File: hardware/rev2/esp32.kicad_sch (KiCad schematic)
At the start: 38 parts, among them J1 SMA, J6 SMA, SW1 SW_Push, SW2 SW_Push, U1 ESP32-S3FN8, Y1 40MHz (±10 ppm, >500 mV)

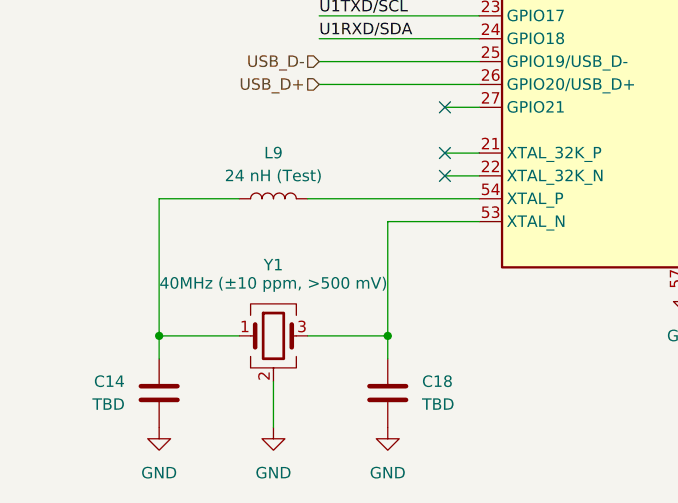
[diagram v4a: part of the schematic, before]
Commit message: added all footprints for esp32 and sx1262, began layouting
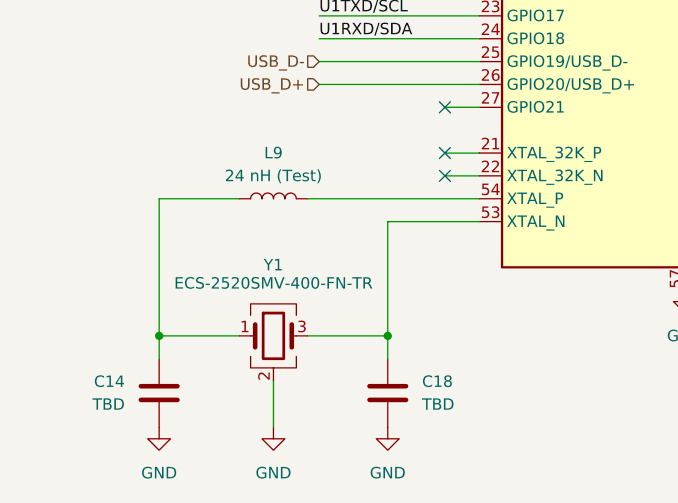
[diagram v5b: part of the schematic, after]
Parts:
- TP1, TP2: footprint (none) -> TestPoint:TestPoint_Pad_D1.0mm
- Y1: value 40MHz (±10 ppm, >500 mV) -> ECS-2520SMV-400-FN-TR; footprint (none) -> Oscillator:Oscillator_SMD_ECS_2520MV-xxx-xx-4Pin_2.5x2.0mm; Mouser Part Number (none) -> 520-EC2520SMV400FNTR

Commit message: continued routing and layouting
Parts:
- renumbered C13 to C11, C17 to C12, C14 to C13, C15 to C14, C21 to C15, C18 to C17, C19 to C18, C20 to C19, C22 to C20, C23 to C21, C24 to C22, C26 to C23, C25 to C24, C27 to C25, J1 to J7, R14 to R10, R15 to R11, R16 to R12, R12 to R13, R19 to R14, R20 to R15, R21 to R16, R4 to R6, R17 to R7, R1 to R8, R13 to R9, SW2 to SW1, SW1 to SW2, U1 to U2

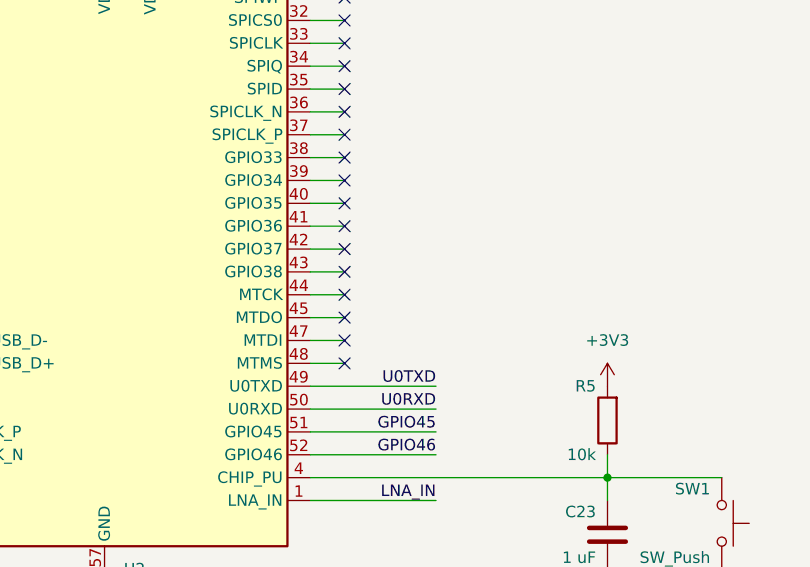
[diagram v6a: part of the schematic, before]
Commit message: finished routing most of the RF and power for SX1262 and ESP32, also decided final ish positions for both.
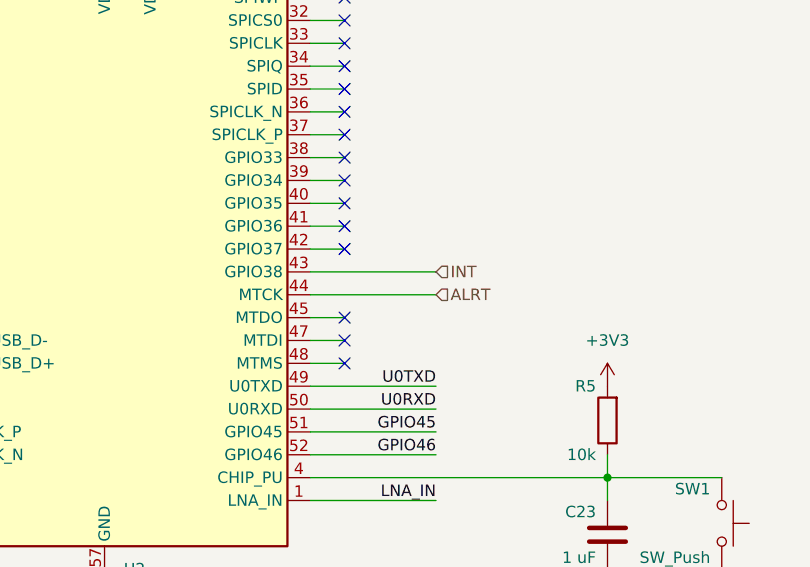
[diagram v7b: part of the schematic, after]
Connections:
- net INT: now reaches U2.43 (GPIO38)
- net ALRT: now reaches U2.44 (MTCK)
- no-connect marks 26 -> 24
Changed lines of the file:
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@@
 	)
 	(no_connect
-		(at 116.84 139.7)
-	)
-	(no_connect
 		(at 116.84 101.6)
 	)
@@
 	)
 	(no_connect
-		(at 116.84 137.16)
-	)
-	(no_connect
 		(at 116.84 147.32)
 	)
@@
 	(wire
 		(pts
-			(xy 113.03 139.7) (xy 116.84 139.7)
+			(xy 113.03 139.7) (xy 127 139.7)
 		)
 		(stroke
@@
 	(wire
 		(pts
-			(xy 113.03 137.16) (xy 116.84 137.16)
+			(xy 113.03 137.16) (xy 127 137.16)
 		)
 		(stroke
@@
 		)
 	)
+	(hierarchical_label "ALRT"
+		(shape input)
+		(at 127 139.7 0)
+		(effects
+			(font
+				(size 1.27 1.27)
+			)
+			(justify left)
+		)
+	)
 	(hierarchical_label "RXD{slash}SDA"
 		(shape input)
@@
 		(effects
 			(font
+				(size 1.27 1.27)
+			)
+			(justify left)
+		)
+	)
+	(hierarchical_label "INT"
+		(shape input)
+		(at 127 137.16 0)
+		(effects
+			(font

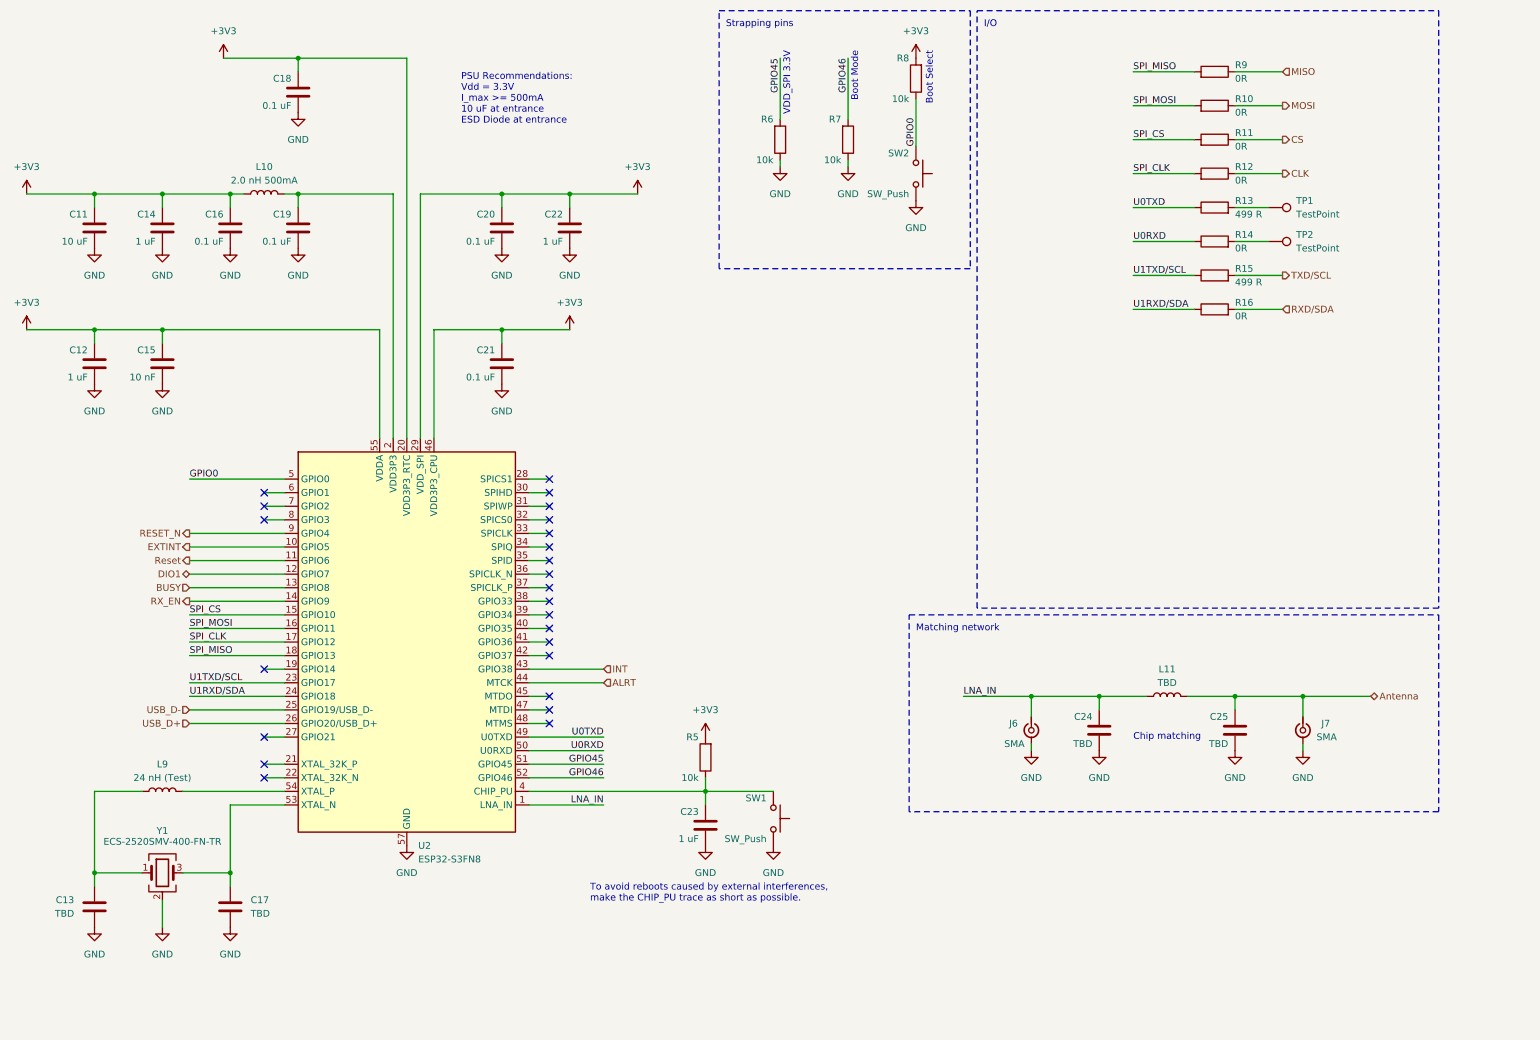
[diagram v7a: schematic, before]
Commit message: routed everything ESP32 and SX1262, will hopefully work. still needs more testpoints
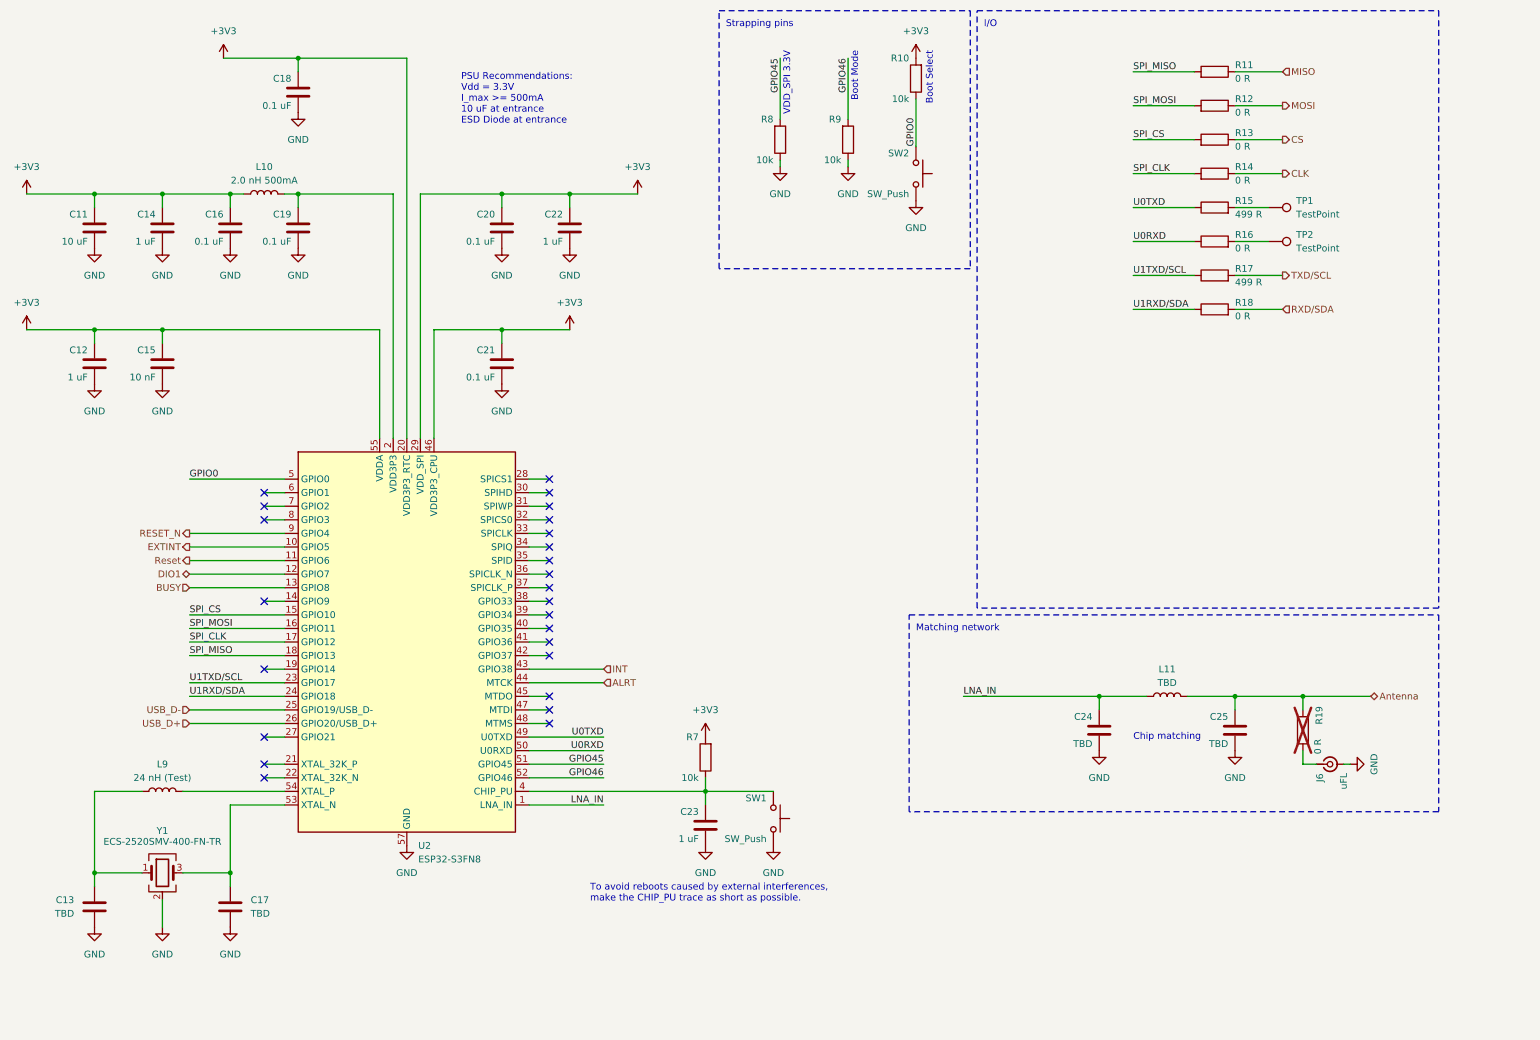
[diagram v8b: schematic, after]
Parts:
- removed J7: SMA, Connector_Coaxial:SMA_Amphenol_132134-16_Vertical, symbol Connector:Conn_Coaxial_Small
- added R19: 0 R, Resistor_SMD:R_0402_1005Metric_Pad0.72x0.64mm_HandSolder, symbol Device:R
- C16, C18, C19, C20, C21: Mouser Part Number 81-GCJ188R71E104KA2D -> 81-GCJ188R71E104KA2D
- J6: value SMA -> uFL; footprint Connector_Coaxial:SMA_Amphenol_132134-16_Vertical -> _footprints:U.FL_Molex_MCRF_73412-0110_Vertical; Mouser Part Number 640-RFPCSMA28F -> 712-CONMHF1-SMD-G-T
- R11: renamed from R9; value 0R -> 0 R; Mouser Part Number (none) -> 71-CRCW0603-0-E3
- R12: renamed from R10; value 0R -> 0 R; Mouser Part Number (none) -> 71-CRCW0603-0-E3
- R13: renamed from R11; value 0R -> 0 R; Mouser Part Number (none) -> 71-CRCW0603-0-E3
- R14: renamed from R12; value 0R -> 0 R; Mouser Part Number (none) -> 71-CRCW0603-0-E3
- R16: renamed from R14; value 0R -> 0 R; Mouser Part Number (none) -> 71-CRCW0603-0-E3
- R18: renamed from R16; value 0R -> 0 R; Mouser Part Number (none) -> 71-CRCW0603-0-E3
- renumbered R8 to R10, R13 to R15, R15 to R17, R5 to R7, R6 to R8, R7 to R9
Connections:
- net Antenna: now also R19.1
- net LNA_IN: no longer J6.1 (In)
- net RX_EN: no longer names the net of U2.14 (GPIO9)
- new net: J6.1 (In), R19.2
- no-connect marks 24 -> 25
